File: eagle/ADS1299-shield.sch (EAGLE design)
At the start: 124 parts, among them IC1 ADS1299IPAG, IC2 TPS72325DBVT, IC3 TPS73225DBVT, IC5 24AA256UID, IC6 TPS604XXDBV, IC7 OPA376DBV, IC8 OPA376DBV, J8 Electrode Connector, U2 TXB0108PWR, U3 TXB0108PWR

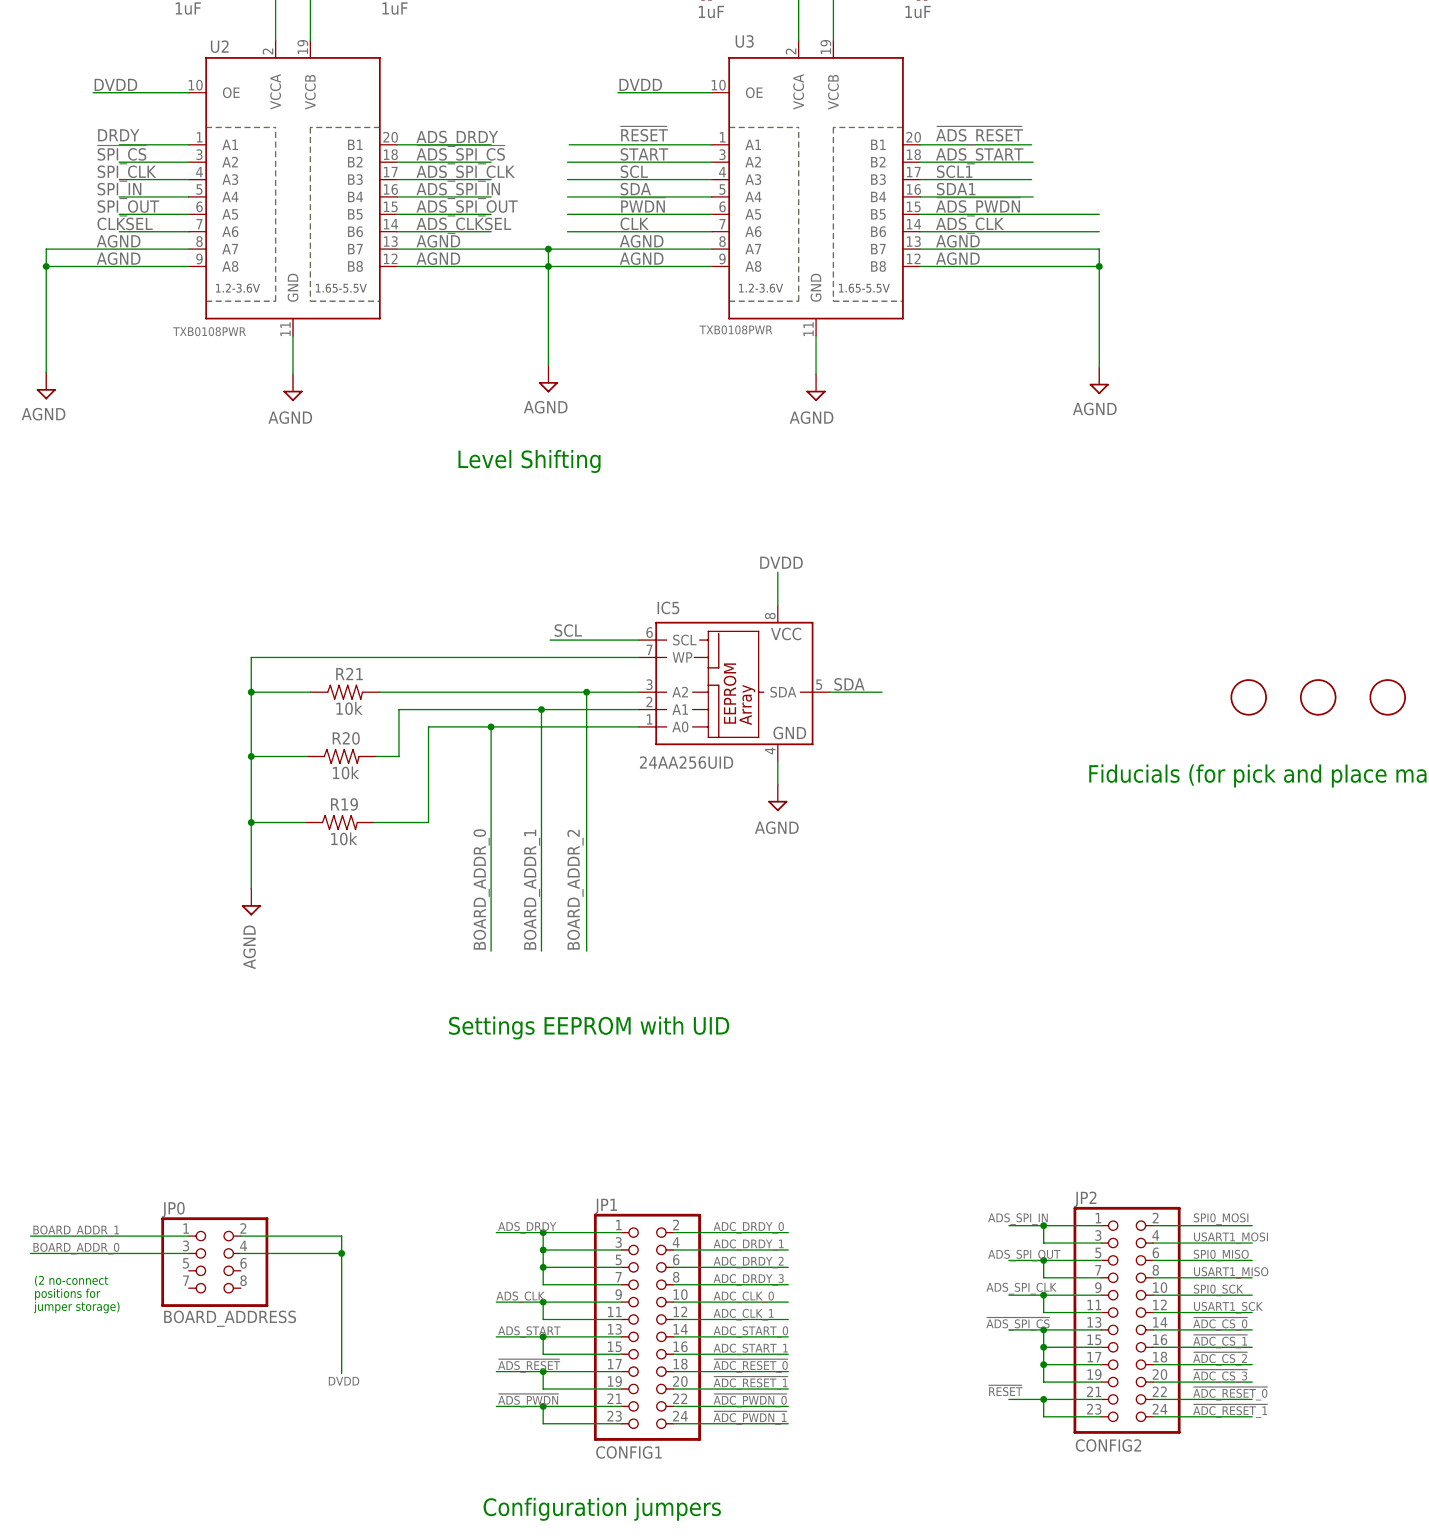
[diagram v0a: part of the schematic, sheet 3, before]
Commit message: new component arrangement - AIN block neat; configuration blocks moved to make more space for routing
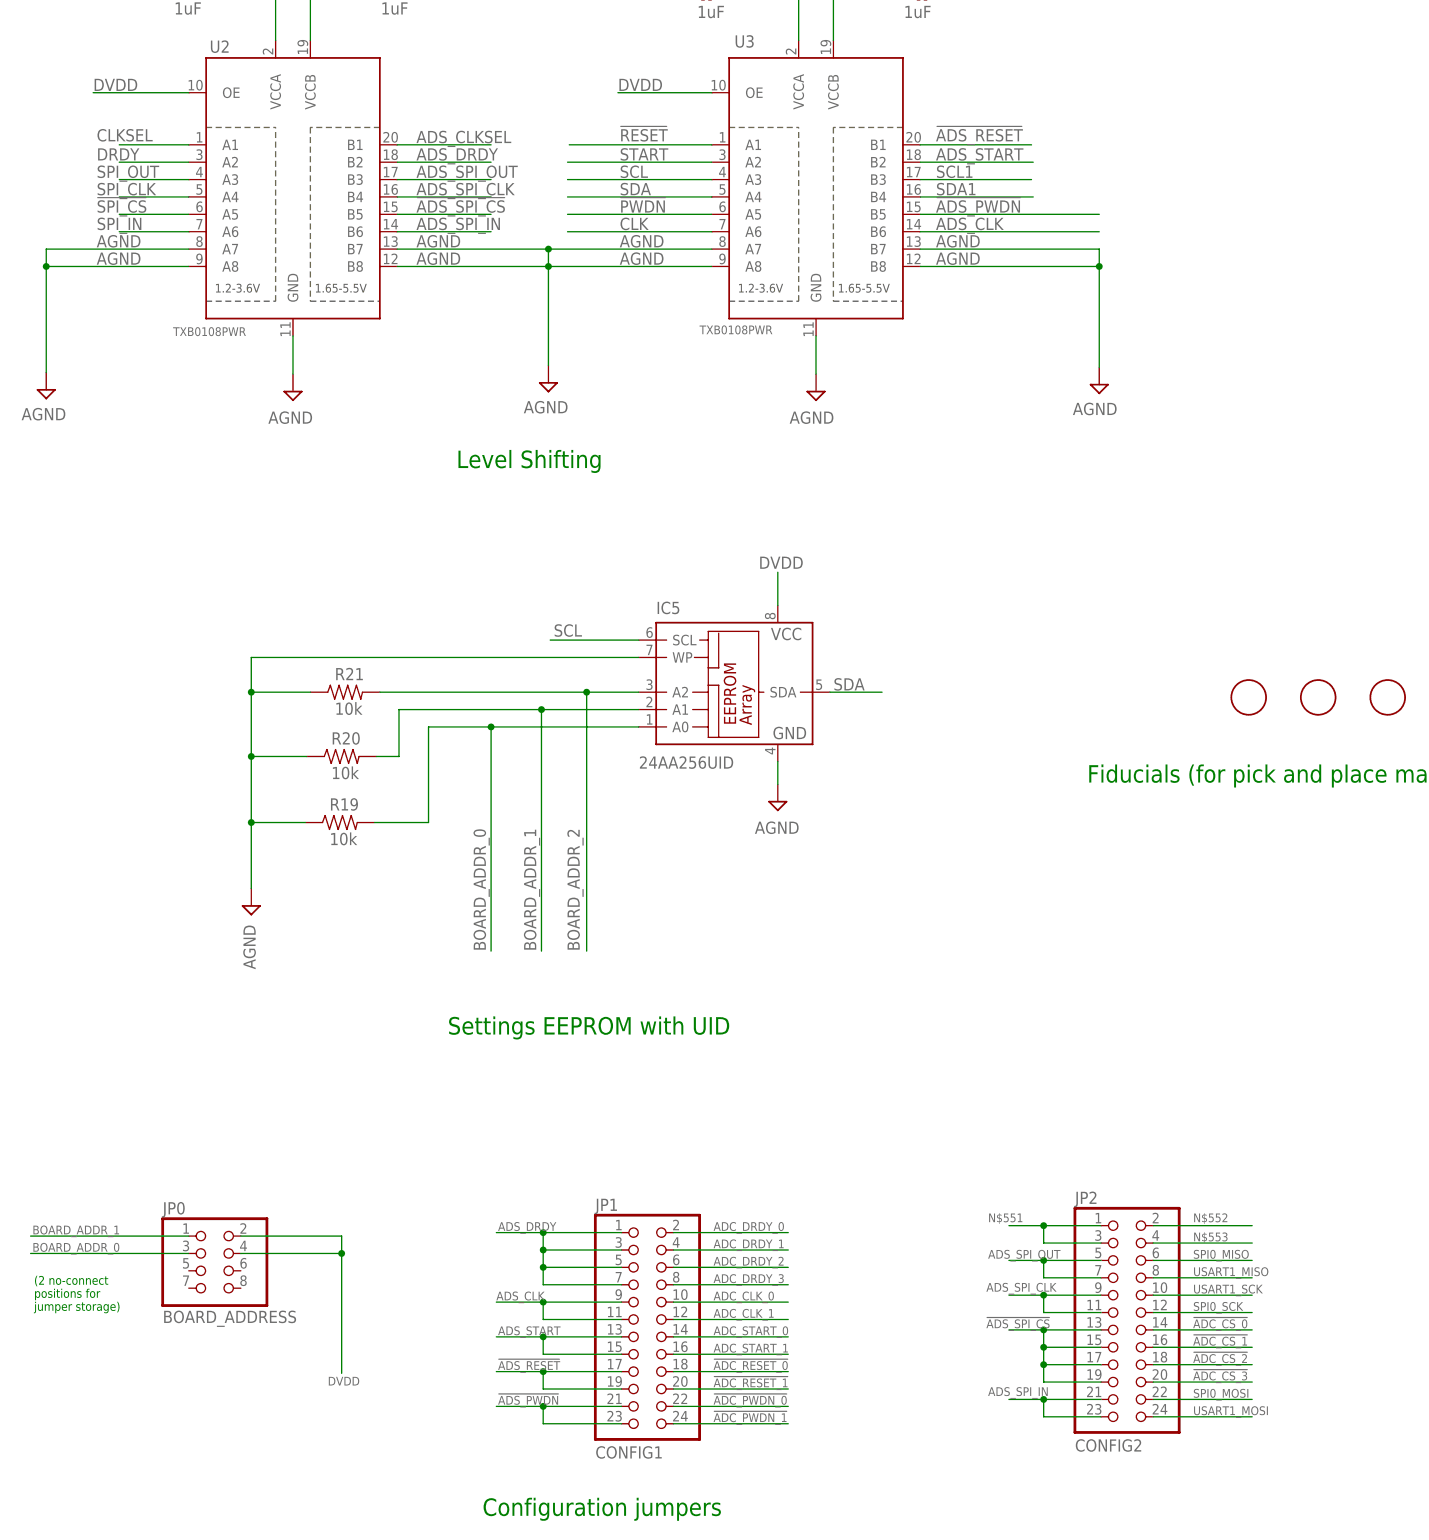
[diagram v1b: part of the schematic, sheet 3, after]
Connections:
- new net N$551: JP2.1, JP2.3
- new net N$552: JP2.2
- new net N$553: JP2.4
- net !ADC_RESET_0: no longer JP2.22
- net !ADC_RESET_1: no longer JP2.24
- net !ADS_SPI_CS: now also U2.B5; no longer U2.B2
- net !RESET: no longer JP2.21, JP2.23
- net !SPI_CS: now also U2.A5; no longer U2.A2
- net ADS_CLKSEL: now also U2.B1; no longer U2.B6
- net ADS_DRDY: now also U2.B2; no longer U2.B1
- net ADS_SPI_CLK: now also U2.B4; no longer U2.B3
- net ADS_SPI_IN: now also JP2.21, JP2.23, U2.B6; no longer JP2.1, JP2.3, U2.B4
- net ADS_SPI_OUT: now also U2.B3; no longer U2.B5
- net CLKSEL: now also U2.A1; no longer U2.A6
- net DRDY: now also U2.A2; no longer U2.A1
- net SPI0_MOSI: now also JP2.22; no longer JP2.2
- net SPI0_SCK: now also JP2.12; no longer JP2.10
- net SPI_CLK: now also U2.A4; no longer U2.A3
- net SPI_IN: now also U2.A6; no longer U2.A4
- net SPI_OUT: now also U2.A3; no longer U2.A5
- net USART1_MOSI: now also JP2.24; no longer JP2.4
- net USART1_SCK: now also JP2.10; no longer JP2.12

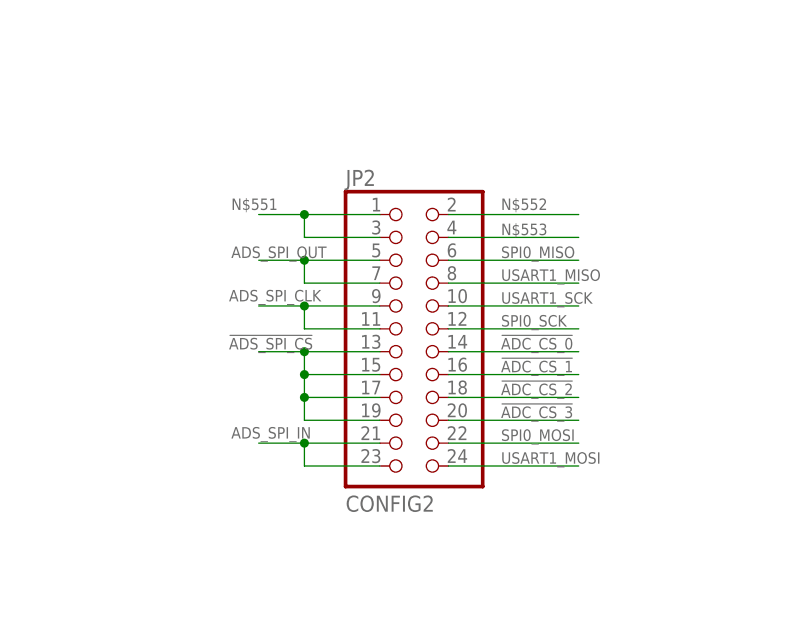
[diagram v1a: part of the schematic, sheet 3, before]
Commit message: updated 2X10 and 2X12 headers to use smaller pads that can route 2 8mil traces between them; routed SPI MOSI, MISO, and CLK to header pins
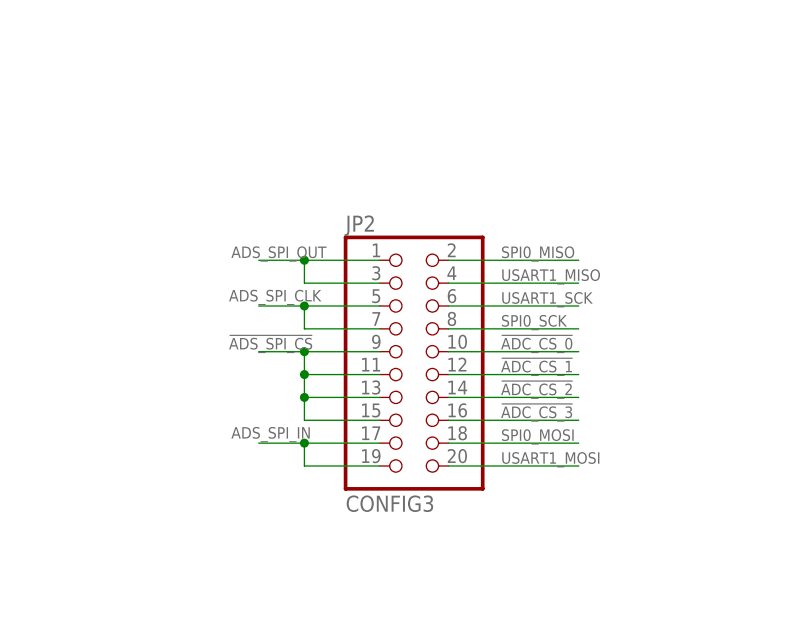
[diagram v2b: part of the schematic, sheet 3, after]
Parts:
- JP2: value CONFIG2 -> CONFIG3; device pin-headers:PINHD-2X12 -> headers:PINHD-2X10
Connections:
- removed net N$551: JP2.1, JP2.3
- removed net N$552: JP2.2
- removed net N$553: JP2.4
- net !ADC_CS_0: now also JP2.10; no longer JP2.14
- net !ADC_CS_1: now also JP2.12; no longer JP2.16
- net !ADC_CS_2: now also JP2.14; no longer JP2.18
- net !ADC_CS_3: now also JP2.16; no longer JP2.20
- net !ADS_SPI_CS: now also JP2.11, JP2.9; no longer JP2.17, JP2.19
- net ADS_SPI_CLK: now also JP2.5, JP2.7; no longer JP2.11, JP2.9
- net ADS_SPI_IN: now also JP2.17, JP2.19; no longer JP2.21, JP2.23
- net ADS_SPI_OUT: now also JP2.1, JP2.3; no longer JP2.5, JP2.7
- net SPI0_MISO: now also JP2.2; no longer JP2.6
- net SPI0_MOSI: now also JP2.18; no longer JP2.22
- net SPI0_SCK: now also JP2.8; no longer JP2.12
- net USART1_MISO: now also JP2.4; no longer JP2.8
- net USART1_MOSI: now also JP2.20; no longer JP2.24
- net USART1_SCK: now also JP2.6; no longer JP2.10
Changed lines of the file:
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@@
 <part name="SUPPLY41" library="supply2" deviceset="AGND" device=""/>
 <part name="SUPPLY42" library="supply2" deviceset="AGND" device=""/>
-<part name="JP2" library="pin-headers" deviceset="PINHD-2X12" device="" value="CONFIG2"/>
 <part name="JP1" library="headers" deviceset="PINHD-2X12" device="" value="CONFIG1"/>
 <part name="JP0" library="headers" deviceset="PINHD-2X4" device="" value="BOARD_ADDRESS"/>
@@
 <part name="SUPPLY51" library="supply2" deviceset="AGND" device=""/>
 <part name="JP16" library="adafruit" deviceset="JST_3PIN" device="" value="EXTERNAL_SYNC"/>
+<part name="JP2" library="headers" deviceset="PINHD-2X10" device="" value="CONFIG3"/>
 </parts>
 <sheets>
@@
 <instance part="FRAME4" gate="G$1" x="0" y="0"/>
 <instance part="FRAME4" gate="G$2" x="322.58" y="0"/>
-<instance part="JP2" gate="A" x="198.12" y="43.18"/>
 <instance part="U2" gate="G$1" x="76.2" y="210.312" smashed="yes">
 <attribute name="NAME" x="64.008" y="228.854" size="1.778" layer="95"/>
@@
 </instance>
 <instance part="JP16" gate="G$1" x="275.336" y="33.02"/>
+<instance part="JP2" gate="A" x="198.12" y="40.894"/>
 </instances>
 <busses>
@@
 </segment>
 <segment>
-<pinref part="JP2" gate="A" pin="21"/>
 <wire x1="194.31" y1="32.004" x2="185.928" y2="32.004" width="0.1524" layer="91"/>
 <label x="177.8" y="32.512" size="1.27" layer="95"/>
-<pinref part="JP2" gate="A" pin="23"/>
 <wire x1="185.928" y1="32.004" x2="180.848" y2="32.004" width="0.1524" layer="91"/>
 <wire x1="194.31" y1="29.464" x2="185.928" y2="29.464" width="0.1524" layer="91"/>
 <wire x1="185.928" y1="29.464" x2="185.928" y2="32.004" width="0.1524" layer="91"/>
 <junction x="185.928" y="32.004"/>
+<pinref part="JP2" gate="A" pin="17"/>
+<pinref part="JP2" gate="A" pin="19"/>
 </segment>
 </net>
 <net name="ADS_SPI_OUT" class="0">
 <segment>
-<pinref part="JP2" gate="A" pin="7"/>
 <wire x1="194.31" y1="49.784" x2="185.928" y2="49.784" width="0.1524" layer="91"/>
-<pinref part="JP2" gate="A" pin="5"/>
 <wire x1="194.31" y1="52.324" x2="185.928" y2="52.324" width="0.1524" layer="91"/>
 <wire x1="185.928" y1="52.324" x2="185.928" y2="49.784" width="0.1524" layer="91"/>
@@
 <wire x1="185.928" y1="52.324" x2="180.848" y2="52.324" width="0.1524" layer="91"/>
 <label x="177.8" y="52.578" size="1.27" layer="95"/>
+<pinref part="JP2" gate="A" pin="1"/>
+<pinref part="JP2" gate="A" pin="3"/>
 </segment>
 <segment>
@@
 <net name="ADS_SPI_CLK" class="0">
 <segment>
-<pinref part="JP2" gate="A" pin="9"/>
 <wire x1="194.31" y1="47.244" x2="185.928" y2="47.244" width="0.1524" layer="91"/>
-<pinref part="JP2" gate="A" pin="11"/>
 <wire x1="194.31" y1="44.704" x2="185.928" y2="44.704" width="0.1524" layer="91"/>
 <wire x1="185.928" y1="47.244" x2="185.928" y2="44.704" width="0.1524" layer="91"/>
@@
 <junction x="185.928" y="47.244"/>
 <label x="177.546" y="47.752" size="1.27" layer="95"/>
+<pinref part="JP2" gate="A" pin="5"/>
+<pinref part="JP2" gate="A" pin="7"/>
 </segment>
 <segment>
@@
 </segment>
 <segment>
-<pinref part="JP2" gate="A" pin="22"/>
 <wire x1="201.93" y1="32.004" x2="216.408" y2="32.004" width="0.1524" layer="91"/>
 <label x="207.772" y="32.258" size="1.27" layer="95"/>
+<pinref part="JP2" gate="A" pin="18"/>
 </segment>
 </net>
@@
 </segment>
 <segment>
-<pinref part="JP2" gate="A" pin="24"/>
 <wire x1="201.93" y1="29.464" x2="216.408" y2="29.464" width="0.1524" layer="91"/>
 <label x="207.772" y="29.718" size="1.27" layer="95"/>
+<pinref part="JP2" gate="A" pin="20"/>
 </segment>
 </net>
 <net name="SPI0_MISO" class="0">
 <segment>
-<pinref part="JP2" gate="A" pin="6"/>
 <wire x1="201.93" y1="52.324" x2="216.408" y2="52.324" width="0.1524" layer="91"/>
 <label x="207.772" y="52.578" size="1.27" layer="95"/>
+<pinref part="JP2" gate="A" pin="2"/>
 </segment>
 <segment>
@@
 <segment>
 <label x="207.772" y="37.338" size="1.27" layer="95"/>
-<pinref part="JP2" gate="A" pin="18"/>
 <wire x1="201.93" y1="37.084" x2="216.408" y2="37.084" width="0.1524" layer="91"/>
+<pinref part="JP2" gate="A" pin="14"/>
 </segment>
 <segment>
@@
 <net name="!ADC_CS_0" class="0">
 <segment>
-<pinref part="JP2" gate="A" pin="14"/>
 <wire x1="201.93" y1="42.164" x2="216.408" y2="42.164" width="0.1524" layer="91"/>
 <label x="207.772" y="42.418" size="1.27" layer="95"/>
+<pinref part="JP2" gate="A" pin="10"/>
 </segment>
 <segment>
@@
 </segment>
 <segment>
-<pinref part="JP2" gate="A" pin="10"/>
 <wire x1="201.93" y1="47.244" x2="216.408" y2="47.244" width="0.1524" layer="91"/>
 <label x="207.772" y="47.498" size="1.27" layer="95"/>
+<pinref part="JP2" gate="A" pin="6"/>
 </segment>
 </net>
 <net name="USART1_MISO" class="0">
 <segment>
-<pinref part="JP2" gate="A" pin="8"/>
 <wire x1="201.93" y1="49.784" x2="216.408" y2="49.784" width="0.1524" layer="91"/>
 <label x="207.772" y="50.038" size="1.27" layer="95"/>
+<pinref part="JP2" gate="A" pin="4"/>
 </segment>
 <segment>
@@
 </segment>
 <segment>
-<pinref part="JP2" gate="A" pin="12"/>
 <wire x1="201.93" y1="44.704" x2="216.408" y2="44.704" width="0.1524" layer="91"/>
 <label x="207.772" y="44.958" size="1.27" layer="95"/>
+<pinref part="JP2" gate="A" pin="8"/>
 </segment>
 </net>
@@
 <net name="!ADC_CS_1" class="0">
 <segment>
-<pinref part="JP2" gate="A" pin="16"/>
 <wire x1="201.93" y1="39.624" x2="216.408" y2="39.624" width="0.1524" layer="91"/>
 <label x="207.772" y="39.878" size="1.27" layer="95"/>
+<pinref part="JP2" gate="A" pin="12"/>
 </segment>
 <segment>
@@
 <net name="!ADC_CS_3" class="0">
 <segment>
-<pinref part="JP2" gate="A" pin="20"/>
 <wire x1="201.93" y1="34.544" x2="216.408" y2="34.544" width="0.1524" layer="91"/>
 <label x="207.772" y="34.798" size="1.27" layer="95"/>
+<pinref part="JP2" gate="A" pin="16"/>
 </segment>
 <segment>
@@
 <net name="!ADS_SPI_CS" class="0">
 <segment>
-<pinref part="JP2" gate="A" pin="13"/>
 <wire x1="194.31" y1="42.164" x2="185.928" y2="42.164" width="0.1524" layer="91"/>
-<pinref part="JP2" gate="A" pin="15"/>
 <wire x1="194.31" y1="39.624" x2="185.928" y2="39.624" width="0.1524" layer="91"/>
 <wire x1="185.928" y1="42.164" x2="185.928" y2="39.624" width="0.1524" layer="91"/>
-<pinref part="JP2" gate="A" pin="17"/>
 <wire x1="194.31" y1="37.084" x2="185.928" y2="37.084" width="0.1524" layer="91"/>
 <wire x1="185.928" y1="39.624" x2="185.928" y2="37.084" width="0.1524" layer="91"/>
 <junction x="185.928" y="39.624"/>
-<pinref part="JP2" gate="A" pin="19"/>
 <wire x1="194.31" y1="34.544" x2="185.928" y2="34.544" width="0.1524" layer="91"/>
 <wire x1="185.928" y1="37.084" x2="185.928" y2="34.544" width="0.1524" layer="91"/>
@@
 <junction x="185.928" y="42.164"/>
 <label x="177.546" y="42.418" size="1.27" layer="95"/>
+<pinref part="JP2" gate="A" pin="9"/>
+<pinref part="JP2" gate="A" pin="11"/>
+<pinref part="JP2" gate="A" pin="13"/>
+<pinref part="JP2" gate="A" pin="15"/>
 </segment>
 <segment>
@@
 </segment>
 </net>
-<net name="N$551" class="0">
-<segment>
-<pinref part="JP2" gate="A" pin="1"/>
-<wire x1="194.31" y1="57.404" x2="185.928" y2="57.404" width="0.1524" layer="91"/>
-<pinref part="JP2" gate="A" pin="3"/>
-<wire x1="194.31" y1="54.864" x2="185.928" y2="54.864" width="0.1524" layer="91"/>
-<wire x1="185.928" y1="57.404" x2="185.928" y2="54.864" width="0.1524" layer="91"/>
-<wire x1="185.928" y1="57.404" x2="180.848" y2="57.404" width="0.1524" layer="91"/>
-<junction x="185.928" y="57.404"/>
-<label x="177.8" y="57.912" size="1.27" layer="95"/>
-</segment>
-</net>
-<net name="N$552" class="0">
-<segment>
-<pinref part="JP2" gate="A" pin="2"/>
-<wire x1="201.93" y1="57.404" x2="216.408" y2="57.404" width="0.1524" layer="91"/>
-<label x="207.772" y="57.912" size="1.27" layer="95"/>
-</segment>
-</net>
-<net name="N$553" class="0">
-<segment>
-<pinref part="JP2" gate="A" pin="4"/>
-<wire x1="201.93" y1="54.864" x2="216.408" y2="54.864" width="0.1524" layer="91"/>
-<label x="207.772" y="55.118" size="1.27" layer="95"/>
-</segment>
-</net>
